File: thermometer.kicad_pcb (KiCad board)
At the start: 2 copper layers, 46 x 46 mm, 51 parts, among them J1 Display, J2 USB, J3 Battery, J4 Programming, J5 DS18B20, SW1 SW_Push, U1 STM32F072CBTx, U2 MCP73831-2-OT, U3 TPS2115, U4 LDS3985M33R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

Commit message: Finished board
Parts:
- moved RV1 15.9 mm to (64.1, 77.9), turned to 90 degrees
- moved R11 9.23 mm to (62.6, 65.3), turned to 180 degrees
- moved R12 5.63 mm to (62.8, 71.4), turned to 0 degrees
- moved U3 5.49 mm to (64.9, 68.4)
- moved C20 4.94 mm to (71.2, 73.4)
- moved U2 4.85 mm to (68.3, 73.2), turned to 90 degrees
- moved F1 3.45 mm to (71.9, 67.8)
- moved D1 2.57 mm to (76.5, 68.8)
- moved C14 2.21 mm to (78.4, 68.9)
- moved C15 2.18 mm to (80.6, 69.1)
- moved C17 1.19 mm to (89.2, 68.0)
- moved C19 1.17 mm to (89.4, 71.9)
- moved C16 1.17 mm to (84.8, 71.8)
- moved C18 1.17 mm to (89.2, 69.8)
- moved U4 1.17 mm to (84.6, 69.0)
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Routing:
- net /DATA: track 0.00 -> 59.5 mm, vias 0 -> 3
- net VBUS: track 0.00 -> 48.4 mm, vias 0 -> 4
- net +BATT: track 0.00 -> 32.1 mm, vias 0 -> 1
- net /CHG_STAT: track 0.00 -> 31.4 mm, vias 0 -> 1
- net /SCL: track 15.2 -> 43.4 mm
- net GND: track 7.83 -> 35.6 mm, vias 6 -> 24
- net /SDA: track 16.1 -> 43.6 mm
- net /POW_STAT: track 2.65 -> 29.7 mm, vias 0 -> 1
- net Net-(C13-Pad1): track 9.71 -> 33.0 mm
- net Net-(C14-Pad1): track 0.00 -> 11.6 mm, vias 0 -> 2
- net Net-(RV1-Pad2): track 0.00 -> 9.23 mm
- net +3V3: track 18.5 -> 25.1 mm
- net Net-(J5-Pad1): track 0.00 -> 5.28 mm
- net Net-(R12-Pad1): track 0.00 -> 4.16 mm
- net Net-(C16-Pad1): track 0.00 -> 3.75 mm
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- added copper zone on F.Cu, net +BATT
- added copper zone on F.Cu, net Net-(C14-Pad1)
- added copper zone on F.Cu, net Net-(F1-Pad2)

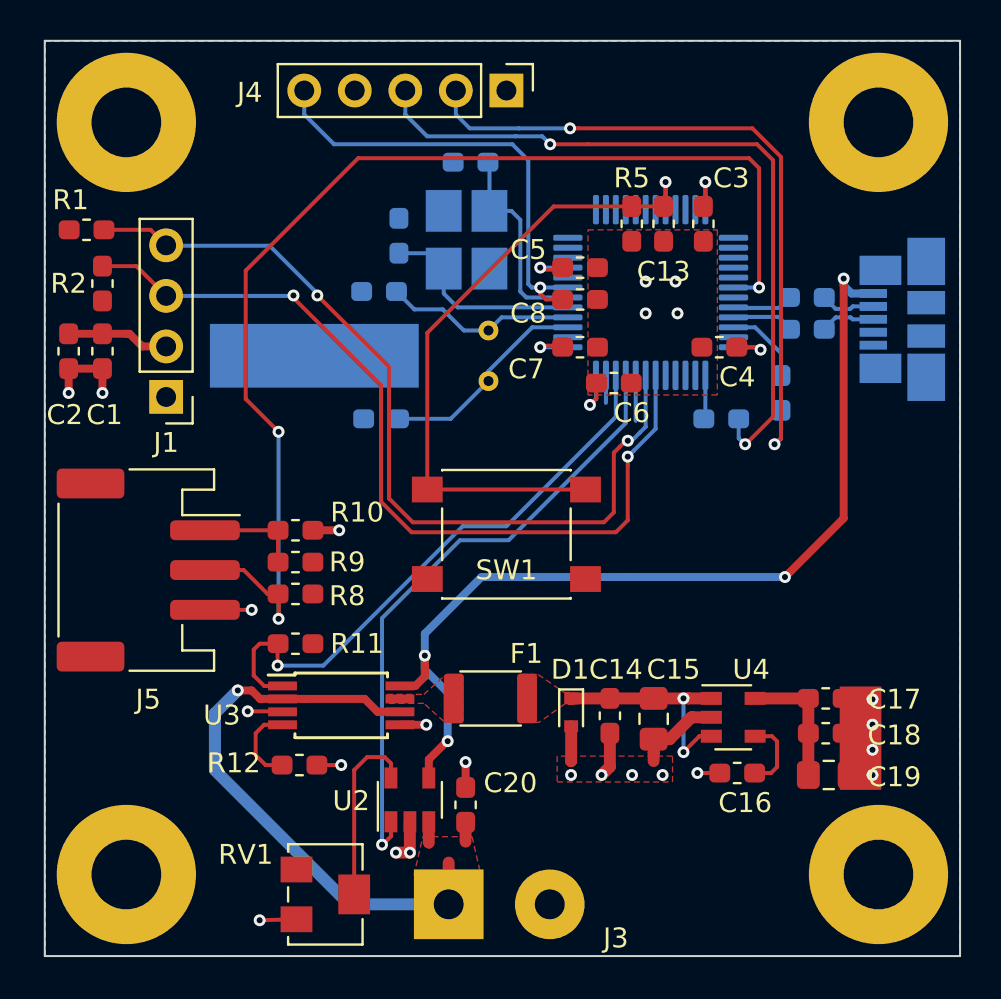
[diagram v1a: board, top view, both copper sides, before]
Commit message: Fixed positions of some elements
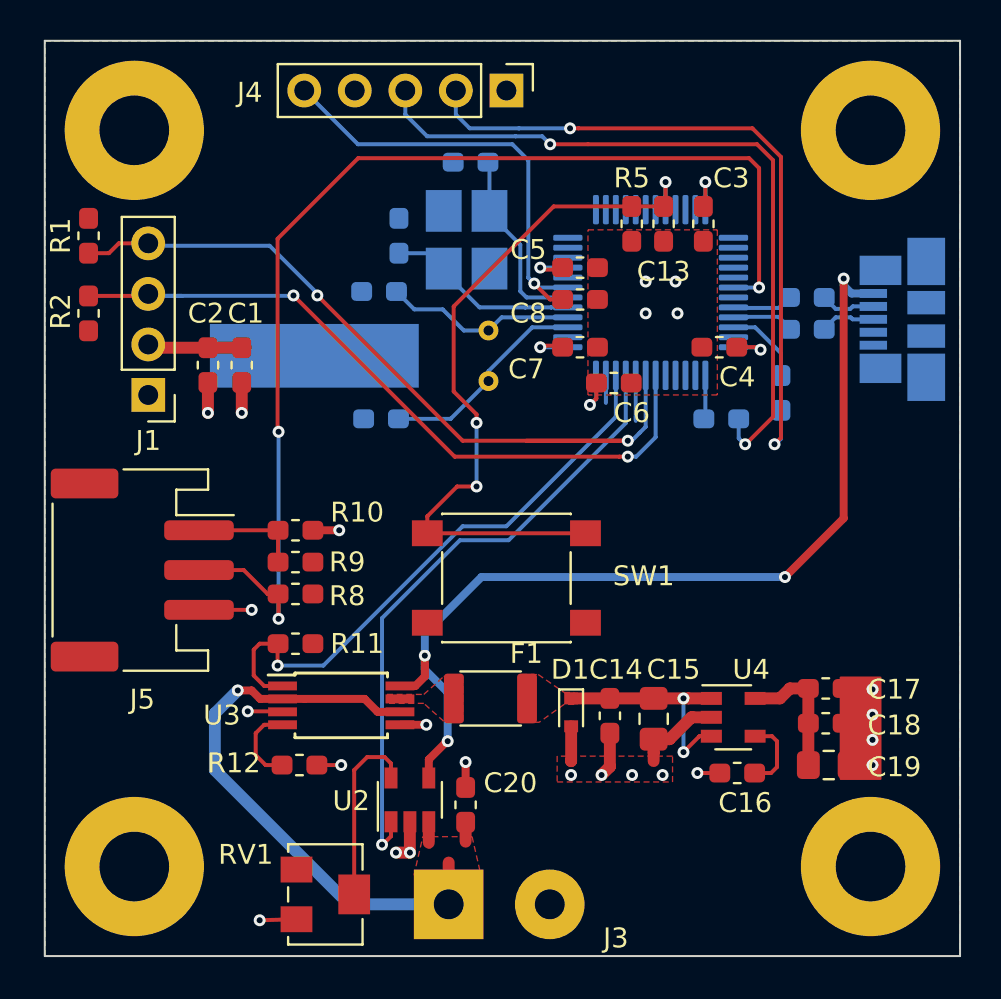
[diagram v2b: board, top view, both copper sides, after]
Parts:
- removed the REF** at (91.9, 76.9)
- removed the REF** at (54.1, 76.9)
- removed the REF** at (91.9, 39.1)
- removed the REF** at (54.1, 39.1)
- added REF**: MountingHole_3.5mm_Pad, MountingHole:MountingHole_3.5mm_Pad, F.Cu at (91.5, 76.5)
- added REF**: MountingHole_3.5mm_Pad, MountingHole:MountingHole_3.5mm_Pad, F.Cu at (91.5, 39.5)
- added REF**: MountingHole_3.5mm_Pad, MountingHole:MountingHole_3.5mm_Pad, F.Cu at (54.5, 39.5)
- added e: MountingHole_3.5mm_Pad, MountingHole:MountingHole_3.5mm_Pad, F.Cu at (54.5, 76.5)
- moved C1 7.03 mm to (59.9, 51.3)
- moved C2 7.03 mm to (58.2, 51.3)
- moved SW1 2.20 mm to (73.1, 61.9)
- moved R2 1.66 mm to (52.2, 48.7)
- moved J1 0.91 mm to (55.2, 52.8)
- moved C17 0.50 mm to (89.2, 67.5)
- moved C18 0.50 mm to (89.2, 69.3)
- moved C19 0.50 mm to (89.4, 71.4)
- moved R1 0.32 mm to (52.2, 44.8), turned to 270 degrees
- moved J5 0.30 mm to (54.9, 61.6)
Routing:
- net /SCL: track 43.4 -> 36.0 mm
- net Net-(C13-Pad1): track 33.0 -> 36.7 mm, vias 1 -> 3
- net /SDA: track 43.6 -> 40.4 mm
- net +3V3: track 25.1 -> 26.6 mm
- net /DATA: track 59.5 -> 58.2 mm
- net GND: track 35.6 -> 34.5 mm
- net /NRST: track 23.2 -> 22.6 mm
- net /OSC_OUT: track 10.3 -> 9.68 mm
- net /OSC_IN: track 10.3 -> 9.70 mm

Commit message: Changed button and dcdc placements
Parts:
- C14, C15, C16, C17, C18, C19, C20, D1, F1, R11, R12, U2, U3, U4: moved to B.Cu
- moved R11 16.3 mm to (76.8, 73.4)
- moved C16 14.2 mm to (86.3, 57.7), turned to 0 degrees
- moved SW1 10.1 mm to (73.0, 72.0)
- moved C19 9.12 mm to (91.6, 62.5)
- moved C17 9.11 mm to (91.4, 58.7)
- moved C18 9.04 mm to (91.4, 60.5)
- moved U4 8.21 mm to (86.5, 61.0), turned to 90 degrees
- moved U3 8.19 mm to (72.9, 70.2), turned to 90 degrees
- moved C20 7.81 mm to (63.4, 72.5)
- moved R12 7.18 mm to (69.9, 72.5), turned to 90 degrees
- moved C15 5.05 mm to (83.4, 64.9)
- moved D1 5.05 mm to (79.3, 64.5)
- moved C14 5.05 mm to (81.2, 64.7)
- moved F1 4.56 mm to (74.6, 64.1)
- moved U2 2.26 mm to (66.3, 72.2)
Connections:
- U1 pad 45: /CHG_STAT -> /POW_STAT
- U1 pad 46: /POW_STAT -> /CHG_STAT
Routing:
- net GND: track 34.5 -> 13.8 mm, vias 24 -> 9
- net +BATT: track 32.1 -> 15.0 mm, vias 1 -> 0
- net Net-(C13-Pad1): track 36.7 -> 46.3 mm, vias 3 -> 5
- net VBUS: track 48.4 -> 53.5 mm, vias 4 -> 5
- net Net-(F1-Pad2): track 0.00 -> 3.35 mm
- net +3V3: track 26.6 -> 23.5 mm, vias 5 -> 10
- net /POW_STAT: track 29.7 -> 27.0 mm, vias 1 -> 2
- net Net-(RV1-Pad2): track 9.23 -> 11.1 mm, vias 0 -> 1
- net Net-(C16-Pad1): track 3.75 -> 1.93 mm
- net Net-(C14-Pad1): track 11.6 -> 12.3 mm
- net /CHG_STAT: track 31.4 -> 32.0 mm, vias 1 -> 2
- added copper zone on B.Cu, net +3V3
- added copper zone on B.Cu, net +BATT
- added copper zone on B.Cu, net Net-(C14-Pad1)
- added copper zone on B.Cu, net Net-(F1-Pad2)
- removed copper zone on F.Cu, net +BATT
- removed copper zone on F.Cu, net Net-(C14-Pad1)
- removed copper zone on F.Cu, net Net-(F1-Pad2)
